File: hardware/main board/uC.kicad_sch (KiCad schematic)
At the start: 19 parts, among them IC1 STM32WB55RGV6, Y1 X322516MLB4SI

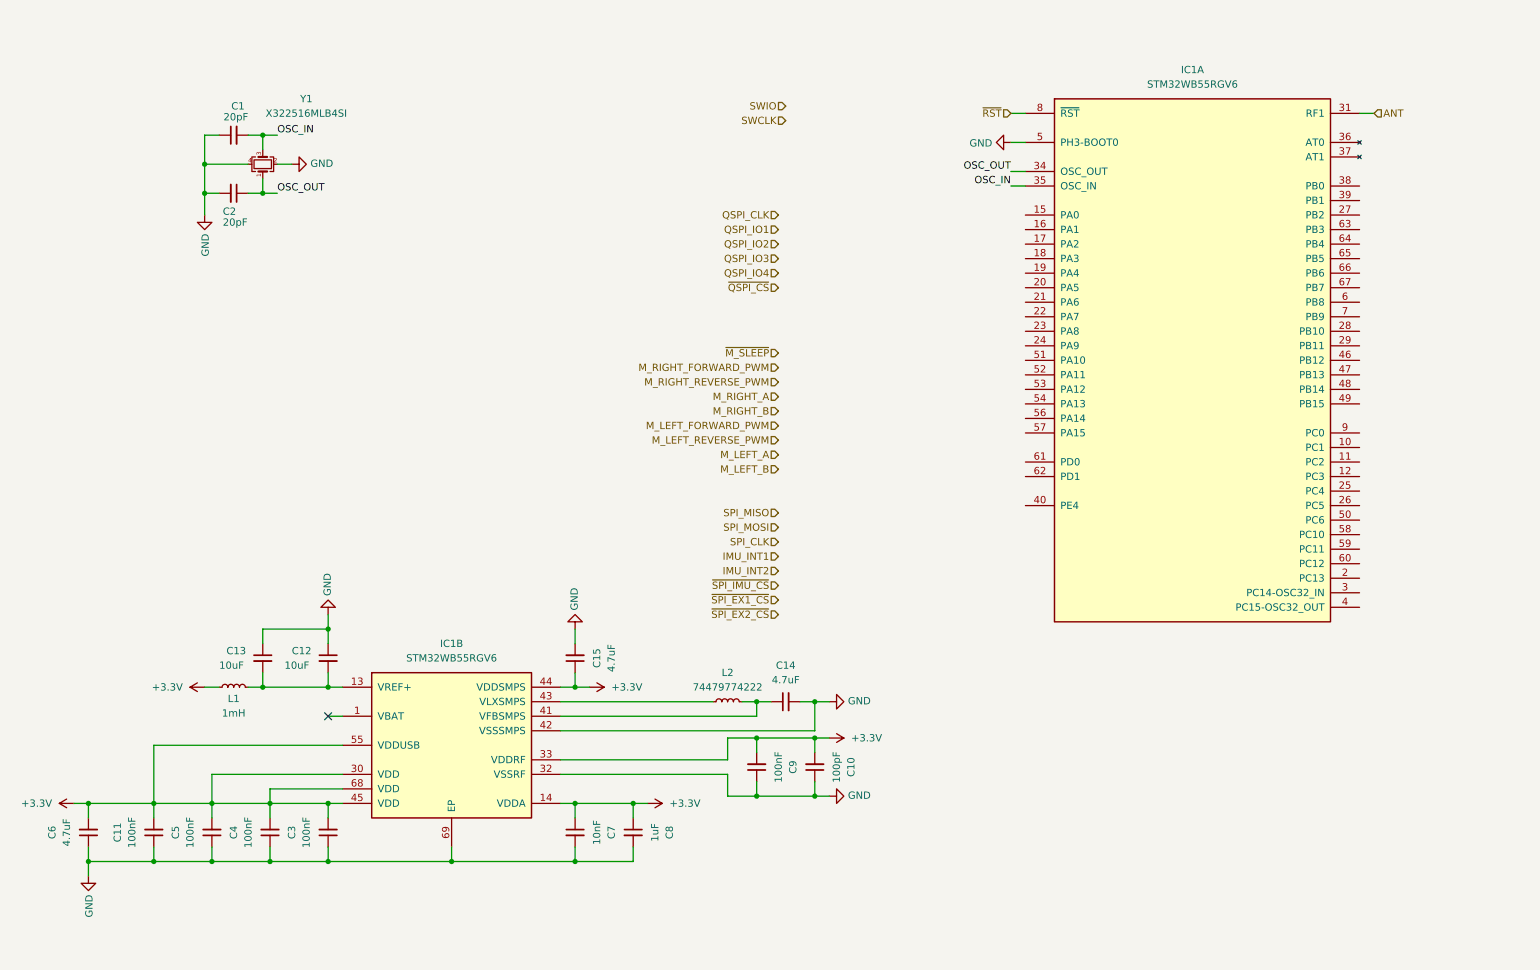
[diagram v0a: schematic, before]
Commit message: main board done, added front board projec
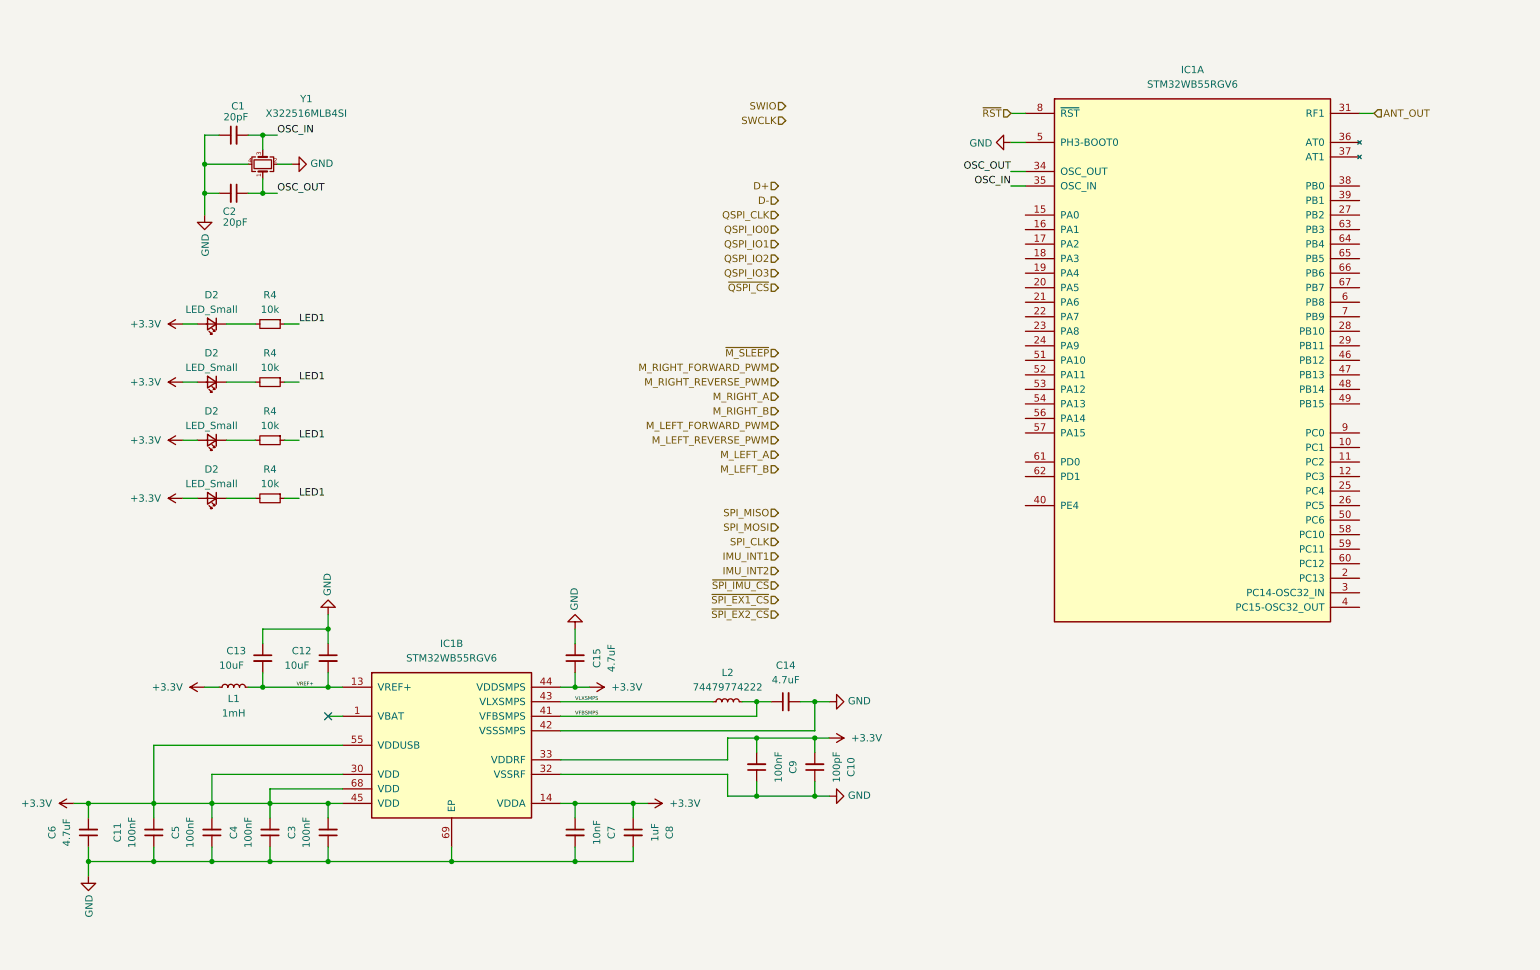
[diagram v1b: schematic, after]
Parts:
- added D2 (x4): LED_Small, LED_SMD:LED_0603_1608Metric, symbol Device:LED_Small
- added R4 (x4): 10k, Resistor_SMD:R_0603_1608Metric, symbol Device:R_Small
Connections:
- net +3.3V: now also D2.2 (A), D2.2 (A), D2.2 (A), D2.2 (A)
- net VREF+: now reaches C12.2, C13.2, IC1.13 (VREF+), L1.2
- net VLXSMPS: now reaches IC1.43 (VLXSMPS), L2.1
- net VFBSMPS: now reaches C14.1, IC1.41 (VFBSMPS), L2.2
- net ANT renamed ANT_OUT
- new net: D2.1 (K), R4.2 (x4)
- new net LED1: R4.1, R4.1, R4.1, R4.1

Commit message: front board schematic done
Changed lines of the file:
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@@
     (effects (font (size 1.27 1.27)) (justify right))
   )
-  (hierarchical_label "SPI_CLK" (shape input) (at 151.13 119.38 180) (fields_autoplaced)
+  (hierarchical_label "SPI_EX_INT2" (shape input) (at 151.13 121.92 180) (fields_autoplaced)
+    (effects (font (size 1.27 1.27)) (justify right))
+  )
+  (hierarchical_label "SPI_EX_INT1" (shape input) (at 151.13 124.46 180) (fields_autoplaced)
+    (effects (font (size 1.27 1.27)) (justify right))
+  )
+  (hierarchical_label "SPI_CLK" (shape input) (at 151.13 114.3 180) (fields_autoplaced)
     (effects (font (size 1.27 1.27)) (justify right))
   )
@@
     (effects (font (size 1.27 1.27)) (justify right))
   )
-  (hierarchical_label "SPI_MISO" (shape input) (at 151.13 114.3 180) (fields_autoplaced)
+  (hierarchical_label "SPI_MISO" (shape input) (at 151.13 109.22 180) (fields_autoplaced)
     (effects (font (size 1.27 1.27)) (justify right))
   )
@@
     (effects (font (size 1.27 1.27)) (justify right))
   )
-  (hierarchical_label "SPI_MOSI" (shape input) (at 151.13 116.84 180) (fields_autoplaced)
+  (hierarchical_label "SPI_MOSI" (shape input) (at 151.13 111.76 180) (fields_autoplaced)
     (effects (font (size 1.27 1.27)) (justify right))
   )
@@
     (effects (font (size 1.27 1.27)) (justify right))
   )
-  (hierarchical_label "IMU_INT2" (shape input) (at 151.13 124.46 180) (fields_autoplaced)
+  (hierarchical_label "IMU_INT2" (shape input) (at 151.13 119.38 180) (fields_autoplaced)
     (effects (font (size 1.27 1.27)) (justify right))
   )
@@
     (effects (font (size 1.27 1.27)) (justify left))
   )
-  (hierarchical_label "IMU_INT1" (shape input) (at 151.13 121.92 180) (fields_autoplaced)
+  (hierarchical_label "IMU_INT1" (shape input) (at 151.13 116.84 180) (fields_autoplaced)
     (effects (font (size 1.27 1.27)) (justify right))
   )

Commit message: all layouts and routings done
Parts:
- removed C12: 10uF, Capacitor_SMD:C_0603_1608Metric, symbol Device:C_Small
- removed C6: 4.7uF, Capacitor_SMD:C_0603_1608Metric, symbol Device:C_Small
- added R4 (x3): 10k, Resistor_SMD:R_0603_1608Metric, symbol Device:R_Small
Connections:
- net D+: now also IC1.53 (PA12)
- net D-: now also IC1.52 (PA11)
- net GND: now also R4.1
- net IMU_INT1: now also IC1.12 (PC3)
- net IMU_INT2: now also IC1.40 (PE4)
- net LED1: now also IC1.15 (PA0); no longer R4.1, R4.1, R4.1
- net M_LEFT_A: now also IC1.9 (PC0)
- net M_RIGHT_A: now also IC1.39 (PB1)
- net QSPI_CLK: now also IC1.18 (PA3)
- net QSPI_IO0: now also IC1.7 (PB9)
- net QSPI_IO1: now also IC1.6 (PB8)
- net QSPI_IO2: now also IC1.22 (PA7)
- net QSPI_IO3: now also IC1.21 (PA6)
- net SPI_CLK: now also IC1.63 (PB3)
- net SPI_EX_INT1: now also IC1.60 (PC12)
- net SPI_EX_INT2: now also IC1.61 (PD0)
- net SPI_MISO: now also IC1.64 (PB4)
- net SPI_MOSI: now also IC1.65 (PB5)
- net SWCLK: now also IC1.56 (PA14)
- net ~{M_SLEEP}: now also IC1.38 (PB0)
- net ~{QSPI_CS}: now also IC1.17 (PA2)
- net ~{SPI_EX1_CS}: now also IC1.58 (PC10)
- net ~{SPI_EX2_CS}: now also IC1.59 (PC11)
- net ~{SPI_IMU_CS}: now also IC1.67 (PB7)
- net VBAT: now reaches IC1.11 (PC2)
- net VBAT: now also R4.1, R4.2
- net LED2: now reaches IC1.16 (PA1)
- net LED2: now also R4.1
- net M_LEFT_PWM: now reaches IC1.23 (PA8)
- net M_LEFT_DIRECTION: now reaches IC1.24 (PA9)
- net LED3: now reaches IC1.26 (PC5)
- net LED3: now also R4.1
- net LED4: now reaches IC1.27 (PB2)
- net LED4: now also R4.1
- net UART_RX: now reaches IC1.28 (PB10)
- net UART_TX: now reaches IC1.29 (PB11)
- net M_RIGHT_DIRECTION: now reaches IC1.50 (PC6)
- net M_RIGHT_PWM: now reaches IC1.51 (PA10)
- net SWDIO: now reaches IC1.54 (PA13)
- new net: R4.1, R4.2
- new net +BATT: R4.2
- no-connect marks 1 -> 15
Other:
- moved on the sheet: C1, C10, C11, C13, C14, C15, C2, C3, C4, C5, C7, C8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

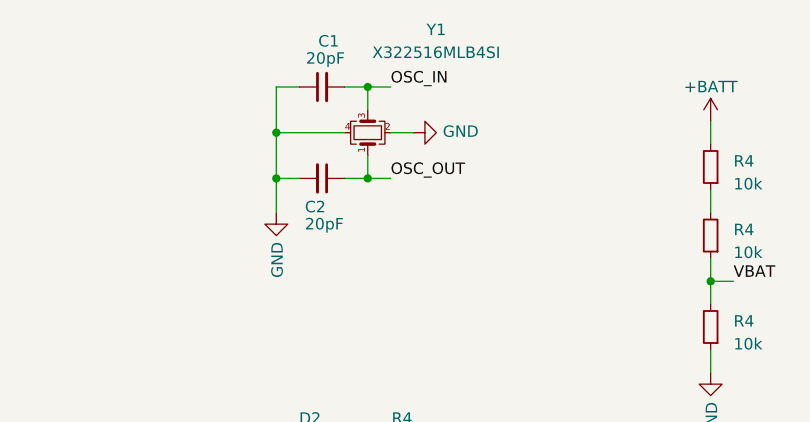
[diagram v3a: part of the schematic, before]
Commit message: firmware - added common classes
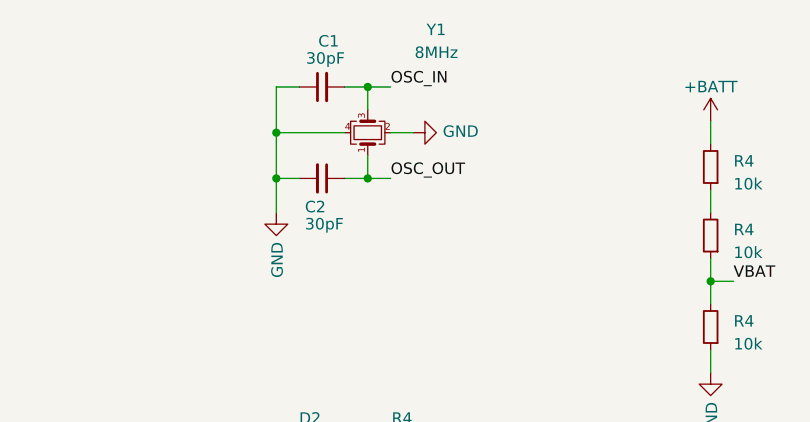
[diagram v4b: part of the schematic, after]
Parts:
- C1, C2: value 20pF -> 30pF; Dodane do zamówienia (none) -> 4; Mouser Part Number (none) -> 80-C0603C300F3HAUTO; Mouser Price/Stock (none) -> https://www.mouser.pl/ProductDetail/KEMET/C0603C300F3HACAUT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
- C10: Dodane do zamówienia (none) -> 10; Mouser Part Number (none) -> 603-CC603KRX7R7BB101; Mouser Price/Stock (none) -> https://www.mouser.pl/ProductDetail/YAGEO/CC0603KRX7R7BB101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
- C11, C3, C4, C5, C9: Dodane do zamówienia (none) -> 20; Mouser Part Number (none) -> 963-EMK107B7104MA-T; Mouser Price/Stock (none) -> https://www.mouser.pl/ProductDetail/TAIYO-YUDEN/EMK107B7104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
- C13: Dodane do zamówienia (none) -> 2; Mouser Part Number (none) -> 81-GRM188R61C106MALJ; Mouser Price/Stock (none) -> https://www.mouser.pl/ProductDetail/Murata-Electronics/GRM1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
- C14, C15: Dodane do zamówienia (none) -> 10; Mouser Part Number (none) -> 187-CL10A475KO8NNNC; Mouser Price/Stock (none) -> https://www.mouser.pl/ProductDetail/Samsung-Electro-Mechani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
- C7: Dodane do zamówienia (none) -> 10; Mouser Part Number (none) -> 80-C0603C103M4RAUTO; Mouser Price/Stock (none) -> https://www.mouser.pl/ProductDetail/KEMET/C0603C103M4RACAUT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
- C8: Dodane do zamówienia (none) -> 10; Mouser Part Number (none) -> 963-EMK107BJ105MAHT; Mouser Price/Stock (none) -> https://www.mouser.pl/ProductDetail/TAIYO-YUDEN/EMK107BJ105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
- D2: Dodane do zamówienia (none) -> 20; Mouser Part Number (none) -> --different--
- IC1, L1, L2: Dodane do zamówienia (none) -> 1
- R4: Dodane do zamówienia (none) -> 10; Mouser Part Number (none) -> CRGCQ0603F10K; Mouser Price/Stock (none) -> https://www.mouser.pl/ProductDetail/TE-Connectivity-Holswor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
- Y1: value X322516MLB4SI -> 8MHz; Dodane do zamówienia (none) -> 1; Mouser Part Number (none) -> ECS-80-20-33-JEN-TR3; Mouser Price/Stock (none) -> https://www.mouser.pl/ProductDetail/ECS/ECS-80-20-33-JEN-TR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
